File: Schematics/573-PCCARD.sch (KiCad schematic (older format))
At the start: 4 parts

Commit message: Fixed bugs
IDE Retrace, PCMCIA checked
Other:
- moved on the sheet: C?B

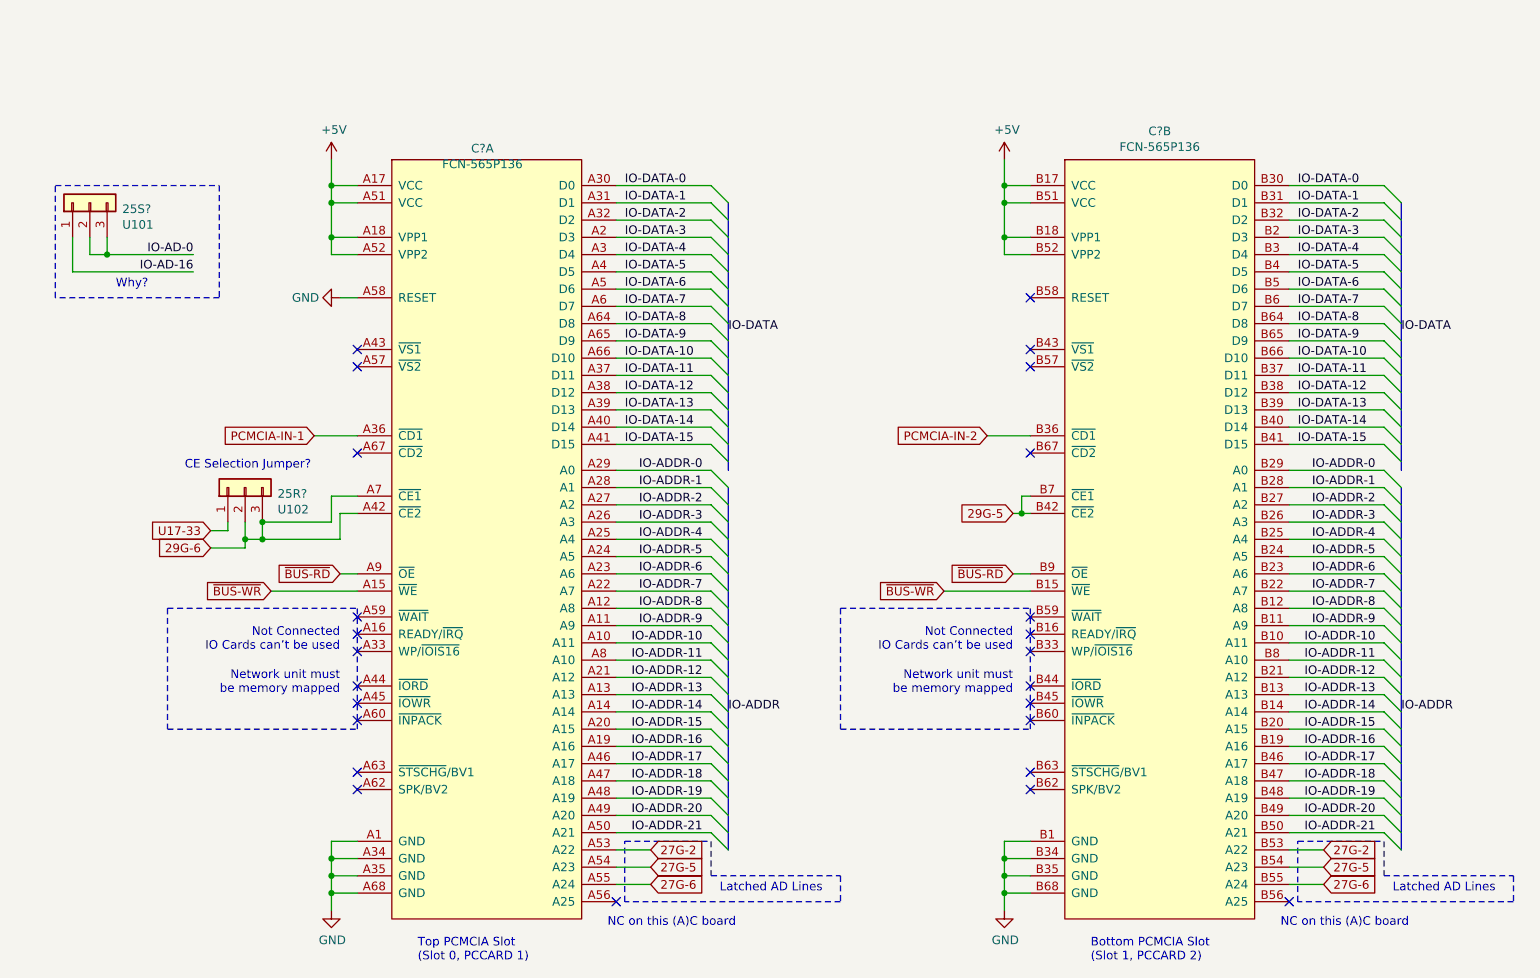
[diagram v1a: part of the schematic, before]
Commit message: Flash fixes, security cart done, most logic figured
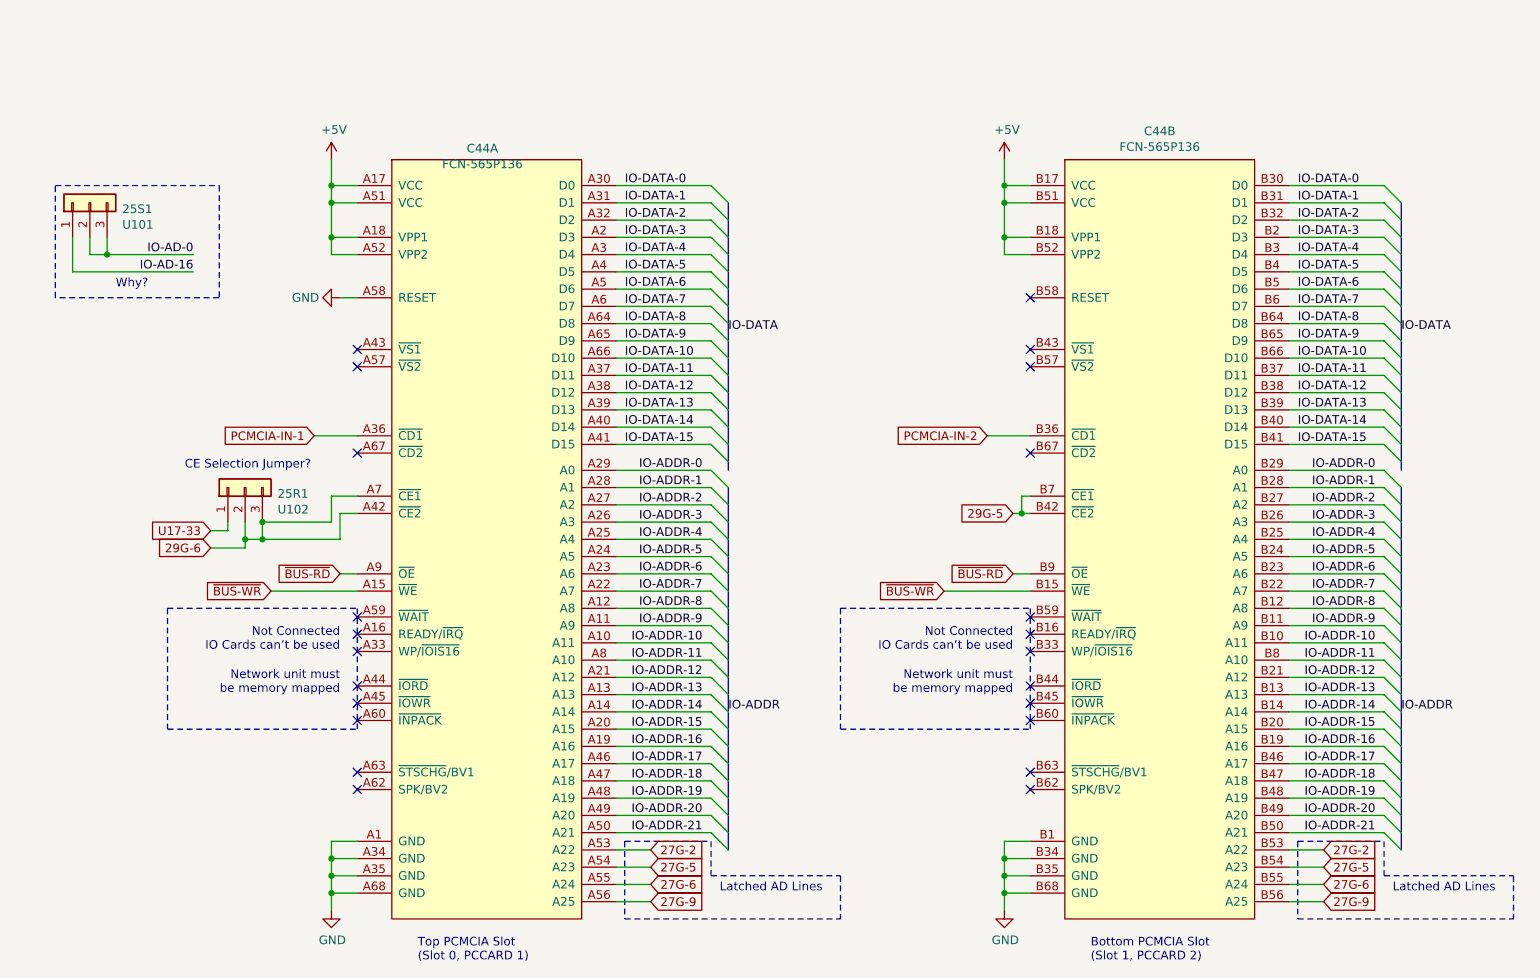
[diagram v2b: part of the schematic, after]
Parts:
- gave numbers to parts that had none: 3
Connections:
- net 27G-9: now reaches C44.A56 (A25)
- net 27G-9: now also C44.B56 (A25)
- no-connect marks 25 -> 23
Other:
- note removed: "NC on this (A)C board"
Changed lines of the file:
@@
 P 3950 3650
 AR Path="/62CF9562/688AD7D0" Ref="C?"  Part="1"
-AR Path="/68891422/688AD7D0" Ref="C?"  Part="1"
-F 0 "C?" H 3925 6065 50  0000 C CNN
+AR Path="/68891422/688AD7D0" Ref="C44"  Part="1"
+F 0 "C44" H 3925 6065 50  0000 C CNN
 F 1 "FCN-565P136" H 3925 5974 50  0000 C CNN
 F 2 "" H 5300 2350 50  0001 C CNN
@@
 P 3050 1300
 AR Path="/62CF9562/688AD7D6" Ref="#PWR?"  Part="1"
-AR Path="/68891422/688AD7D6" Ref="#PWR?"  Part="1"
-F 0 "#PWR?" H 3050 1150 50  0001 C CNN
+AR Path="/68891422/688AD7D6" Ref="#PWR0242"  Part="1"
+F 0 "#PWR0242" H 3050 1150 50  0001 C CNN
 F 1 "+5V" H 3065 1473 50  0000 C CNN
 F 2 "" H 3050 1300 50  0001 C CNN
@@
 P 3050 5650
 AR Path="/62CF9562/688AD7DC" Ref="#PWR?"  Part="1"
-AR Path="/68891422/688AD7DC" Ref="#PWR?"  Part="1"
-F 0 "#PWR?" H 3050 5400 50  0001 C CNN
+AR Path="/68891422/688AD7DC" Ref="#PWR0243"  Part="1"
+F 0 "#PWR0243" H 3050 5400 50  0001 C CNN
 F 1 "GND" H 3055 5477 50  0000 C CNN
 F 2 "" H 3050 5650 50  0001 C CNN
@@
 P 6950 1300
 AR Path="/62CF9562/688AD807" Ref="#PWR?"  Part="1"
-AR Path="/68891422/688AD807" Ref="#PWR?"  Part="1"
-F 0 "#PWR?" H 6950 1150 50  0001 C CNN
+AR Path="/68891422/688AD807" Ref="#PWR0244"  Part="1"
+F 0 "#PWR0244" H 6950 1150 50  0001 C CNN
 F 1 "+5V" H 6965 1473 50  0000 C CNN
 F 2 "" H 6950 1300 50  0001 C CNN
@@
 P 6950 5650
 AR Path="/62CF9562/688AD80D" Ref="#PWR?"  Part="1"
-AR Path="/68891422/688AD80D" Ref="#PWR?"  Part="1"
-F 0 "#PWR?" H 6950 5400 50  0001 C CNN
+AR Path="/68891422/688AD80D" Ref="#PWR0245"  Part="1"
+F 0 "#PWR0245" H 6950 5400 50  0001 C CNN
 F 1 "GND" H 6955 5477 50  0000 C CNN
 F 2 "" H 6950 5650 50  0001 C CNN
@@
 P 2550 3200
 AR Path="/62CF9562/688AD83C" Ref="25R?"  Part="1"
-AR Path="/68891422/688AD83C" Ref="25R?"  Part="1"
-F 0 "25R?" V 2514 3012 50  0000 R CNN
+AR Path="/68891422/688AD83C" Ref="25R1"  Part="1"
+F 0 "25R1" V 2514 3012 50  0000 R CNN
 F 1 "U102" V 2423 3012 50  0000 R CNN
 F 2 "Connector_PinHeader_2.54mm:PinHeader_1x03_P2.54mm_Vertical" H 2550 3200 50  0001 C CNN
@@
 Wire Wire Line
 	7050 3250 7100 3250
-$Comp
-L Connectors_PC:FCN-565P136 C?
-U 2 1 688AD849
-P 7850 3650
-AR Path="/62CF9562/688AD849" Ref="C?"  Part="2"
-AR Path="/68891422/688AD849" Ref="C?"  Part="2"
-F 0 "C?" H 7850 6165 50  0000 C CNN
-F 1 "FCN-565P136" H 7850 6074 50  0000 C CNN
-F 2 "" H 9200 2350 50  0001 C CNN
-F 3 "" H 9200 2350 50  0001 C CNN
-	2    7850 3650
-	1    0    0    -1
-$EndComp
 NoConn ~ 3200 3000
 Text Notes 3550 5950 0    50   ~ 0
@@
 P 3100 2100
 AR Path="/62CF9562/688AD895" Ref="#PWR?"  Part="1"
-AR Path="/68891422/688AD895" Ref="#PWR?"  Part="1"
-F 0 "#PWR?" H 3100 1850 50  0001 C CNN
+AR Path="/68891422/688AD895" Ref="#PWR0246"  Part="1"
+F 0 "#PWR0246" H 3100 1850 50  0001 C CNN
 F 1 "GND" V 3100 1900 50  0000 C CNN
 F 2 "" H 3100 2100 50  0001 C CNN
@@
 P 1650 1550
 AR Path="/62CF9562/688AD8AA" Ref="25S?"  Part="1"
-AR Path="/68891422/688AD8AA" Ref="25S?"  Part="1"
-F 0 "25S?" V 1614 1362 50  0000 R CNN
+AR Path="/68891422/688AD8AA" Ref="25S1"  Part="1"
+F 0 "25S1" V 1614 1362 50  0000 R CNN
 F 1 "U101" V 1523 1362 50  0000 R CNN
 F 2 "Connector_PinHeader_2.54mm:PinHeader_1x03_P2.54mm_Vertical" H 1650 1550 50  0001 C CNN
@@
 Wire Notes Line
 	6000 3900 7100 3900
-NoConn ~ 4700 5600
 Text GLabel 4900 5500 2    50   Input ~ 0
 27G-6
@@
 Entry Wire Line
 	5350 5300 5250 5200
-Text Notes 4650 5750 0    50   ~ 0
-NC on this (A)C board
 Entry Wire Line
 	9150 1450 9250 1550
@@
 Entry Wire Line
 	9250 5300 9150 5200
-Text Notes 8550 5750 0    50   ~ 0
-NC on this (A)C board
 Text Notes 5300 5550 0    50   ~ 0
 Latched AD Lines
@@
 Wire Notes Line
 	5250 5450 6000 5450
-Wire Notes Line
-	6000 5450 6000 5600
-Wire Notes Line
-	6000 5600 4750 5600
-Wire Notes Line
-	4750 5600 4750 5250
 Text GLabel 8800 5500 2    50   Input ~ 0
 27G-6
@@
 	-200 -8700 -1450 -8700
 Wire Notes Line
-	8650 5600 8650 5250
-NoConn ~ 8600 5600
-Wire Notes Line
 	9150 5450 9900 5450
-Wire Notes Line
-	9900 5450 9900 5600
-Wire Notes Line
-	9900 5600 8650 5600
+$Comp
+L Connectors_PC:FCN-565P136 C?
+U 2 1 688AD849
+P 7850 3650
+AR Path="/62CF9562/688AD849" Ref="C?"  Part="2"
+AR Path="/68891422/688AD849" Ref="C44"  Part="2"
+F 0 "C44" H 7850 6165 50  0000 C CNN
+F 1 "FCN-565P136" H 7850 6074 50  0000 C CNN
+F 2 "" H 9200 2350 50  0001 C CNN
+F 3 "" H 9200 2350 50  0001 C CNN
+	2    7850 3650
+	1    0    0    -1
+$EndComp
+Text GLabel 4900 5600 2    50   Input ~ 0
+27G-9
+Wire Wire Line
+	4900 5600 4700 5600
+Wire Notes Line
+	4750 5700 6000 5700
+Wire Notes Line
+	6000 5450 6000 5700
+Wire Notes Line
+	4750 5250 4750 5700
+Text GLabel 8800 5600 2    50   Input ~ 0
+27G-9
+Wire Notes Line
+	8650 5700 9900 5700
+Wire Notes Line
+	9900 5450 9900 5700
+Wire Wire Line
+	8800 5600 8600 5600
+Wire Notes Line
+	8650 5250 8650 5700
 Wire Bus Line
 	9250 3200 9250 5300
